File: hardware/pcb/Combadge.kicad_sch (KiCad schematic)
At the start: 13 parts, among them J1 Conn_01x05_Female, J3 TOUCH, U2 ESP32-WROOM-32, U4 NAU8315YG

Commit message: Assign some footprints. Not done.
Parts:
- C1, C2, C3, C5, C6: footprint (none) -> Capacitor_SMD:C_1206_3216Metric_Pad1.33x1.80mm_HandSolder
- J1: footprint (none) -> Connector_PinHeader_1.27mm:PinHeader_1x05_P1.27mm_Vertical
- MK1: footprint MIC_CMM-3526D-261-I2S-TR -> (none)
- R1, R5: footprint (none) -> Resistor_SMD:R_1206_3216Metric_Pad1.30x1.75mm_HandSolder
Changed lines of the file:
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@@
       (effects (font (size 1.27 1.27)) (justify left))
     )
-    (property "Footprint" "" (id 2) (at 221.9452 85.09 0)
+    (property "Footprint" "Capacitor_SMD:C_1206_3216Metric_Pad1.33x1.80mm_HandSolder" (id 2) (at 221.9452 85.09 0)
       (effects (font (size 1.27 1.27)) hide)
     )
@@
       (effects (font (size 1.27 1.27)) (justify left))
     )
-    (property "Footprint" "" (id 2) (at 260.096 104.394 90)
+    (property "Footprint" "Resistor_SMD:R_1206_3216Metric_Pad1.30x1.75mm_HandSolder" (id 2) (at 260.096 104.394 90)
       (effects (font (size 1.27 1.27)) hide)
     )
@@
     (property "Reference" "MK1" (id 0) (at 231.14 21.59 0))
     (property "Value" "CMM-3526D-261-I2S-TR" (id 1) (at 231.14 24.13 0))
-    (property "Footprint" "MIC_CMM-3526D-261-I2S-TR" (id 2) (at 231.14 36.83 0)
+    (property "Footprint" "" (id 2) (at 231.14 36.83 0)
       (effects (font (size 1.27 1.27)) (justify left bottom) hide)
     )
@@
       (effects (font (size 1.27 1.27)) (justify left))
     )
-    (property "Footprint" "" (id 2) (at 39.37 179.07 0)
+    (property "Footprint" "Connector_PinHeader_1.27mm:PinHeader_1x05_P1.27mm_Vertical" (id 2) (at 39.37 179.07 0)
       (effects (font (size 1.27 1.27)) hide)
     )
@@
     (property "Reference" "C1" (id 0) (at 50.8 30.48 90))
     (property "Value" "10uF" (id 1) (at 50.8 33.02 90))
-    (property "Footprint" "" (id 2) (at 54.61 25.7048 0)
+    (property "Footprint" "Capacitor_SMD:C_1206_3216Metric_Pad1.33x1.80mm_HandSolder" (id 2) (at 54.61 25.7048 0)
       (effects (font (size 1.27 1.27)) hide)
     )
@@
     (property "Reference" "C2" (id 0) (at 50.8 40.64 90))
     (property "Value" "100pF" (id 1) (at 50.8 43.18 90))
-    (property "Footprint" "" (id 2) (at 54.61 35.8648 0)
+    (property "Footprint" "Capacitor_SMD:C_1206_3216Metric_Pad1.33x1.80mm_HandSolder" (id 2) (at 54.61 35.8648 0)
       (effects (font (size 1.27 1.27)) hide)
     )
@@
       (effects (font (size 1.27 1.27)) (justify left))
     )
-    (property "Footprint" "" (id 2) (at 229.5652 85.09 0)
+    (property "Footprint" "Capacitor_SMD:C_1206_3216Metric_Pad1.33x1.80mm_HandSolder" (id 2) (at 229.5652 85.09 0)
       (effects (font (size 1.27 1.27)) hide)
     )
@@
     (property "Reference" "C3" (id 0) (at 50.8 50.8 90))
     (property "Value" "10uF" (id 1) (at 50.8 53.34 90))
-    (property "Footprint" "" (id 2) (at 54.61 46.0248 0)
+    (property "Footprint" "Capacitor_SMD:C_1206_3216Metric_Pad1.33x1.80mm_HandSolder" (id 2) (at 54.61 46.0248 0)
       (effects (font (size 1.27 1.27)) hide)
     )
@@
     (property "Reference" "R1" (id 0) (at 64.77 40.64 90))
     (property "Value" "10k" (id 1) (at 64.77 43.18 90))
-    (property "Footprint" "" (id 2) (at 64.516 48.006 90)
+    (property "Footprint" "Resistor_SMD:R_1206_3216Metric_Pad1.30x1.75mm_HandSolder" (id 2) (at 64.516 48.006 90)
       (effects (font (size 1.27 1.27)) hide)
     )
@@
     )
     (path "/522738f4-f6b2-4897-a079-07da122bd152/54fa1821-1962-473c-8470-e88a1b27fa8c"
-      (reference "BT1") (unit 1) (value "Battery_Cell") (footprint "Package_DFN_QFN:OnSemi_XDFN4-1EP_1.0x1.0mm_EP0.52x0.52mm")
+      (reference "BT1") (unit 1) (value "Battery_Cell") (footprint "")
     )
     (path "/a446316d-6e49-438a-84a1-cec983c2bc64"
-      (reference "C1") (unit 1) (value "10uF") (footprint "")
+      (reference "C1") (unit 1) (value "10uF") (footprint "Capacitor_SMD:C_1206_3216Metric_Pad1.33x1.80mm_HandSolder")
     )
     (path "/c4358fdf-40af-42ed-9431-23ecd93e8b68"
-      (reference "C2") (unit 1) (value "100pF") (footprint "")
+      (reference "C2") (unit 1) (value "100pF") (footprint "Capacitor_SMD:C_1206_3216Metric_Pad1.33x1.80mm_HandSolder")
     )
     (path "/e7fdbe85-5916-4d9a-a1c4-f3b4768c56a5"
-      (reference "C3") (unit 1) (value "10uF") (footprint "")
+      (reference "C3") (unit 1) (value "10uF") (footprint "Capacitor_SMD:C_1206_3216Metric_Pad1.33x1.80mm_HandSolder")
     )
     (path "/522738f4-f6b2-4897-a079-07da122bd152/f007b42a-a975-49eb-bcc8-b60c81440f04"
-      (reference "C4") (unit 1) (value "1uF") (footprint "")
+      (reference "C4") (unit 1) (value "1uF") (footprint "Capacitor_SMD:C_1206_3216Metric_Pad1.33x1.80mm_HandSolder")
     )
     (path "/45675717-f492-4f4f-a167-18356673890d"
-      (reference "C5") (unit 1) (value "4.7uF") (footprint "")
+      (reference "C5") (unit 1) (value "4.7uF") (footprint "Capacitor_SMD:C_1206_3216Metric_Pad1.33x1.80mm_HandSolder")
     )
     (path "/c9c68790-db29-4468-810c-d11a4b68e482"
-      (reference "C6") (unit 1) (value "100pF") (footprint "")
+      (reference "C6") (unit 1) (value "100pF") (footprint "Capacitor_SMD:C_1206_3216Metric_Pad1.33x1.80mm_HandSolder")
     )
     (path "/522738f4-f6b2-4897-a079-07da122bd152/90b83734-9b32-498c-90f9-3d6e745143bf"
@@
     )
     (path "/a1162625-0ef3-4f3c-9db9-a306a20d12d7"
-      (reference "J1") (unit 1) (value "Conn_01x05_Female") (footprint "")
+      (reference "J1") (unit 1) (value "Conn_01x05_Female") (footprint "Connector_PinHeader_1.27mm:PinHeader_1x05_P1.27mm_Vertical")
     )
     (path "/522738f4-f6b2-4897-a079-07da122bd152/54bad96c-0bd2-4df6-9bda-0db6ccbaa90e"
@@
     )
     (path "/6692667a-23d9-4d51-a0f9-87ae21b84031"
-      (reference "MK1") (unit 1) (value "CMM-3526D-261-I2S-TR") (footprint "MIC_CMM-3526D-261-I2S-TR")
+      (reference "MK1") (unit 1) (value "CMM-3526D-261-I2S-TR") (footprint "")
     )
     (path "/522738f4-f6b2-4897-a079-07da122bd152/e5e4e075-c2c1-4820-852d-89aedf0b3eda"
-      (reference "MOSFET1") (unit 1) (value "SI2342DS-T1-GE3") (footprint "SOT-23_TO-236_VIS")
+      (reference "MOSFET1") (unit 1) (value "SI2342DS-T1-GE3") (footprint "Si2342DS:SI2342DS-T1-GE3")
     )
     (path "/f73ba15a-b5c2-4609-86f3-0cf8c0519475"
-      (reference "R1") (unit 1) (value "10k") (footprint "")
+      (reference "R1") (unit 1) (value "10k") (footprint "Resistor_SMD:R_1206_3216Metric_Pad1.30x1.75mm_HandSolder")
     )
     (path "/522738f4-f6b2-4897-a079-07da122bd152/a541230b-5814-4e7a-9253-410d18d69814"
-      (reference "R2") (unit 1) (value "10k") (footprint "")
+      (reference "R2") (unit 1) (value "10k") (footprint "Resistor_SMD:R_1206_3216Metric_Pad1.30x1.75mm_HandSolder")
     )
     (path "/522738f4-f6b2-4897-a079-07da122bd152/f8a31955-f0f5-470b-a677-0289439ad53d"
-      (reference "R3") (unit 1) (value "10k") (footprint "")
+      (reference "R3") (unit 1) (value "10k") (footprint "Resistor_SMD:R_1206_3216Metric_Pad1.30x1.75mm_HandSolder")
     )
     (path "/522738f4-f6b2-4897-a079-07da122bd152/b6d90d67-d83b-40f3-be35-89fe4de090a8"
-      (reference "R4") (unit 1) (value "10") (footprint "")
+      (reference "R4") (unit 1) (value "10") (footprint "Resistor_SMD:R_1206_3216Metric_Pad1.30x1.75mm_HandSolder")
     )
     (path "/65ecb276-9d69-4f1a-bd2e-69221f373bf0"
-      (reference "R5") (unit 1) (value "100k") (footprint "")
+      (reference "R5") (unit 1) (value "100k") (footprint "Resistor_SMD:R_1206_3216Metric_Pad1.30x1.75mm_HandSolder")
     )
     (path "/522738f4-f6b2-4897-a079-07da122bd152/bd72950c-6810-4eec-8819-388bfc93ab04"
-      (reference "R_ISET1") (unit 1) (value "10k") (footprint "")
+      (reference "R_ISET1") (unit 1) (value "10k") (footprint "Si2342DS:SI2342DS-T1-GE3")
     )
     (path "/522738f4-f6b2-4897-a079-07da122bd152/4d9bfdc9-548c-473b-8b63-b9edd4d05e1e"

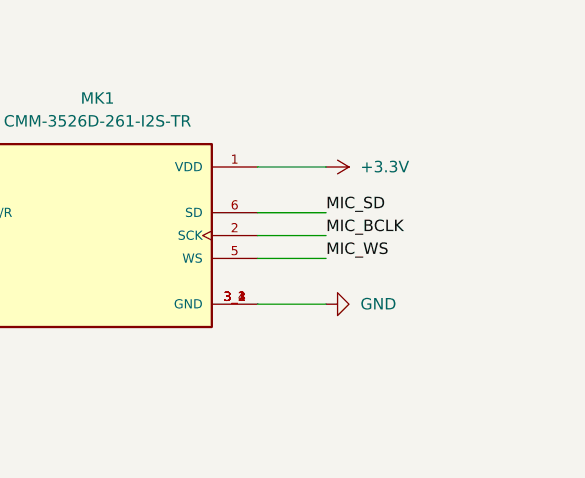
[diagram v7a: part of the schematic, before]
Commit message: Add some decoupling capacitors
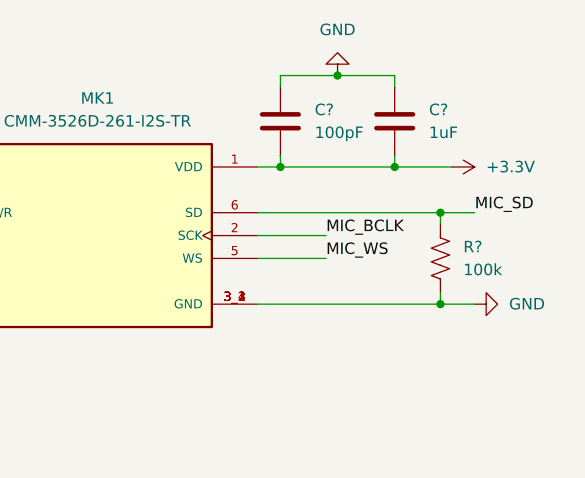
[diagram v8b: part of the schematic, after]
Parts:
- added C?: 1uF, symbol Device:C
- added C?: 100pF, symbol Device:C
- added R?: 100k, symbol Device:R_US
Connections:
- net +3.3V: now also C?.2, C?.2
- net GND: now also C?.1, C?.1, R?.2
- net MIC_SD: now also R?.1
